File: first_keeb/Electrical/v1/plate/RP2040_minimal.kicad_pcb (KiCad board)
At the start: 2 copper layers, 67.2 x 67.2 mm, 9 parts

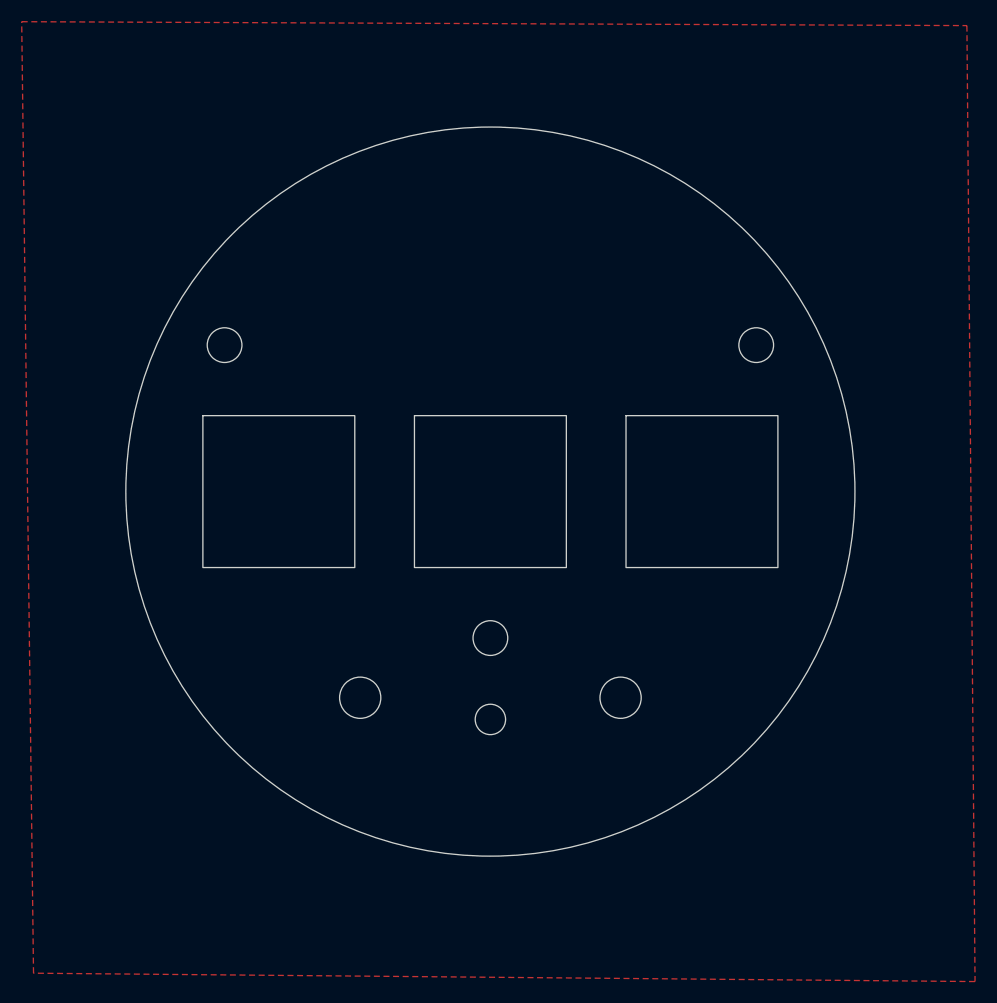
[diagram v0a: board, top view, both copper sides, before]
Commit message: adds pullup for run pin
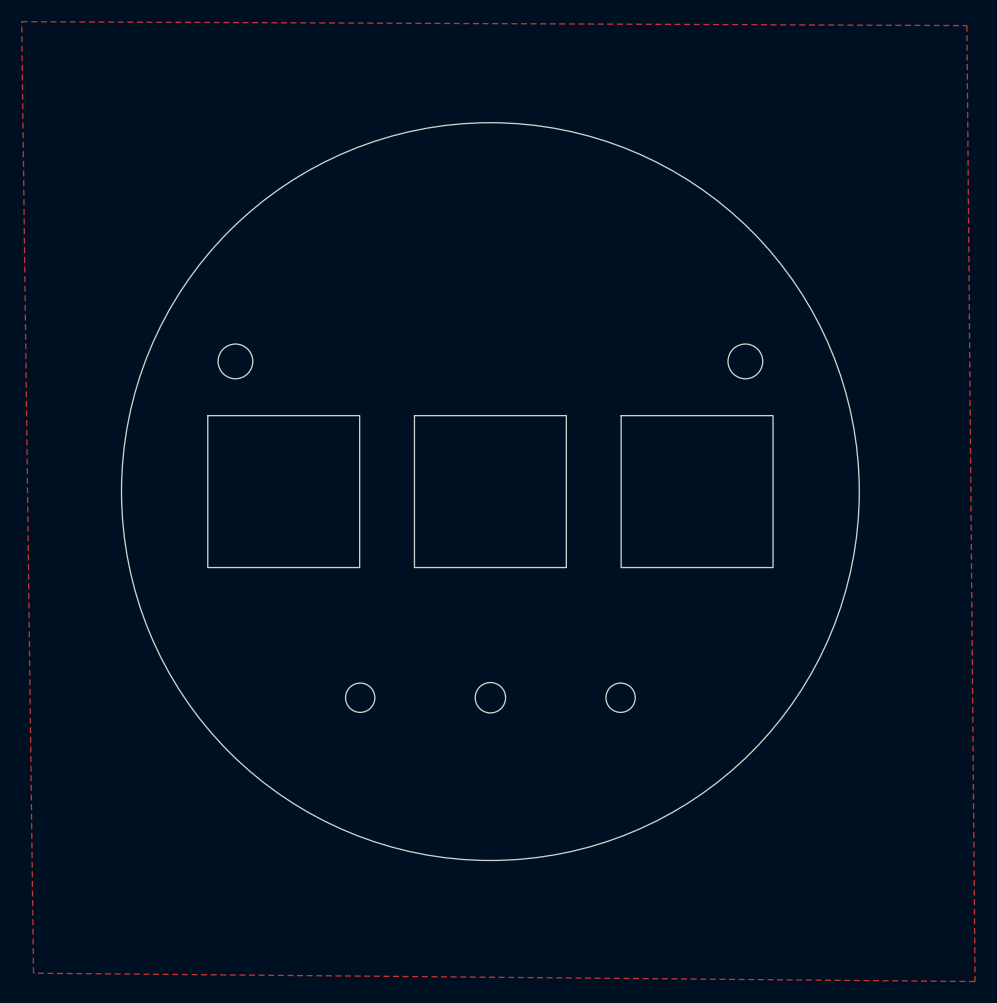
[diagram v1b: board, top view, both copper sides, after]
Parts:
- removed H3: MountingHole_3.2mm_M3, MountingHole:MountingHole_3.2mm_M3
- REF** (x2): value MountingHole_3.7mm -> MountingHole_2.7mm; footprint MountingHole:MountingHole_3.7mm -> MountingHole:MountingHole_2.7mm
- moved REF** 2.00 mm to (100.0, 119.0)
- moved H1 1.80 mm to (76.5, 88.0)
- moved H2 1.80 mm to (123.5, 88.0)
- moved REF** 0.45 mm to (81.0, 100.0)
- moved REF** 0.45 mm to (119.0, 100.0)
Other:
- board size 67.2 x 67.2 mm -> 68 x 68 mm
